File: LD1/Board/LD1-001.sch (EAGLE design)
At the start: 13 parts, among them IC1 TLC5941NT, IC2 TLC5941NT, IC3 TLC5941NT

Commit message: Before the first prototyping.
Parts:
- removed CN2, CN3: (no value), jst-ph:B16B-PH-K-S
- removed SV1: (no value), con-ml:ML10
- added C4: 0.01u, rcl:C-US025-025X050
- added IC4: TLC5941NT, adafruit:TLC5941NT
- added JP1, JP2, JP3, JP4: (no value), pinhead:PINHD-2X16
- added JP5: (no value), pinhead:PINHD-1X2
- added R4: 4.7k, resistor:R-US_0204/5
- CN1: device jst-ph:B16B-PH-K-S -> jst-ph:S8B-PH-K-S
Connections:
- removed net LED2B: CN3.6, IC3.OUT5
- removed net LED2G: CN3.5, IC3.OUT4
- removed net LED3B: CN3.9, IC3.OUT8
- removed net LED3G: CN3.8, IC3.OUT7
- removed net LED3R: CN3.7, IC3.OUT6
- removed net LEDA: CN3.1, IC3.OUT0
- removed net SIN: IC3.SIN, SV1.3
- new net N$37: IC4.IREF, R4.2
- new net N$48: IC3.OUT8, JP3.17
- new net N$49: IC3.OUT9, JP3.19
- new net N$50: IC3.OUT10, JP3.21
- new net N$51: IC3.OUT11, JP3.23
- new net N$52: IC3.OUT12, JP3.25
- new net N$53: IC3.OUT13, JP3.27
- new net N$54: IC3.OUT14, JP3.29
- new net N$55: IC3.OUT15, JP3.31
- new net N$56: IC4.OUT0, JP4.1
- new net N$57: IC4.OUT1, JP4.3
- new net N$58: IC4.OUT2, JP4.5
- new net N$59: IC4.OUT3, JP4.7
- new net N$60: IC4.OUT4, JP4.9
- new net N$61: IC4.OUT5, JP4.11
- new net N$62: IC4.OUT6, JP4.13
- new net N$63: IC4.OUT7, JP4.15
- new net N$64: IC4.OUT8, JP4.17
- new net N$66: IC4.OUT9, JP4.19
- new net N$67: IC4.OUT10, JP4.21
- new net N$68: IC4.OUT11, JP4.23
- new net N$69: IC4.OUT12, JP4.25
- new net N$70: IC4.OUT13, JP4.27
- new net N$71: IC4.OUT14, JP4.29
- new net N$72: IC4.OUT15, JP4.31
- new net N$73: JP1.10, JP1.12, JP1.14, JP1.16, JP1.18, JP1.2, JP1.20, JP1.22, JP1.24, JP1.26, JP1.28, JP1.30, JP1.32, JP1.4, JP1.6, JP1.8, JP2.10, JP2.12, JP2.14, JP2.16, JP2.18, JP2.2, JP2.20, JP2.22, JP2.24, JP2.26, JP2.28, JP2.30, JP2.32, JP2.4, JP2.6, JP2.8, JP3.10, JP3.12, JP3.14, JP3.16, JP3.18, JP3.2, JP3.20, JP3.22, JP3.24, JP3.26, JP3.28, JP3.30, JP3.32, JP3.4, JP3.6, JP3.8, JP4.10, JP4.12, JP4.14, JP4.16, JP4.18, JP4.2, JP4.20, JP4.22, JP4.24, JP4.26, JP4.28, JP4.30, JP4.32, JP4.4, JP4.6, JP4.8, JP5.1
- net BLANK: now also CN1.3, IC4.BLANK; no longer SV1.5
- net GND: now also C4.2, CN1.2, IC4.GND, JP5.2; no longer SV1.10, SV1.2
- net GSCLCK: now also CN1.4, IC4.GSCLK; no longer SV1.7
- net MODE: now also CN1.8, IC4.MODE; no longer SV1.8
- net N$1: now also CN1.6, IC1.SIN; no longer CN2.16, IC2.OUT15
- net N$10: now also IC1.OUT5, JP1.11; no longer IC2.SIN, IC3.SOUT
- net N$11: now also IC1.OUT6, JP1.13; no longer CN2.4, IC2.OUT3
- net N$12: now also IC1.OUT7, JP1.15; no longer CN3.2, IC3.OUT1
- net N$13: now also IC1.OUT8, JP1.17; no longer CN2.5, IC2.OUT4
- net N$14: now also IC1.OUT9, JP1.19; no longer CN3.3, IC3.OUT2
- net N$15: now also IC1.OUT10, JP1.21; no longer CN2.6, IC2.OUT5
- net N$16: now also IC1.OUT11, JP1.23; no longer CN2.7, IC2.OUT6
- net N$17: now also IC1.OUT12, JP1.25; no longer CN2.8, IC2.OUT7
- net N$18: now also IC1.OUT13, JP1.27; no longer CN2.9, IC2.OUT8
- net N$19: now also IC1.OUT14, JP1.29; no longer CN2.10, IC2.OUT9
- net N$2: now also IC1.SOUT, IC2.SIN; no longer CN2.2, IC2.OUT1
- net N$20: now also IC1.OUT15, JP1.31; no longer CN2.11, IC2.OUT10
- net N$21: now also IC2.OUT0, JP2.1; no longer CN2.12, IC2.OUT11
- net N$22: now also IC2.OUT1, JP2.3; no longer CN2.13, IC2.OUT12
- net N$23: now also IC2.OUT2, JP2.5; no longer CN2.14, IC2.OUT13
- net N$24: now also IC2.OUT3, JP2.7; no longer CN3.15, IC3.OUT14
- net N$25: now also IC2.OUT4, JP2.9; no longer CN3.16, IC3.OUT15
- net N$26: now also IC2.OUT5, JP2.11; no longer CN2.15, IC2.OUT14
- net N$27: now also IC2.OUT6, JP2.13; no longer CN2.1, IC2.OUT0
- net N$28: now also IC2.OUT7, JP2.15; no longer CN1.16, IC1.OUT15
- net N$29: now also IC2.OUT8, JP2.17; no longer CN1.15, IC1.OUT14
- net N$3: now also IC2.SOUT, IC3.SIN; no longer CN3.13, IC3.OUT12
- net N$30: now also IC2.OUT9, JP2.19; no longer CN1.14, IC1.OUT13
- net N$31: now also IC2.OUT10, JP2.21; no longer CN1.13, IC1.OUT12
- net N$32: now also IC2.OUT11, JP2.23; no longer CN1.12, IC1.OUT11
- net N$33: now also IC2.OUT12, JP2.25; no longer CN1.11, IC1.OUT10
- net N$34: now also IC2.OUT13, JP2.27; no longer CN1.10, IC1.OUT9
- net N$35: now also IC2.OUT14, JP2.29; no longer CN1.9, IC1.OUT8
- net N$36: now also IC2.OUT15, JP2.31; no longer CN1.8, IC1.OUT7
- net N$38: now also IC3.OUT0, JP3.1; no longer CN1.7, IC1.OUT6
- net N$39: now also IC3.OUT1, JP3.3; no longer CN1.6, IC1.OUT5
- net N$4: now also IC3.SOUT, IC4.SIN; no longer CN2.3, IC2.OUT2
- net N$40: now also IC3.OUT2, JP3.5; no longer CN1.5, IC1.OUT4
- net N$41: now also IC3.OUT3, JP3.7; no longer CN1.4, IC1.OUT3
- net N$42: now also IC3.OUT4, JP3.9; no longer CN1.3, IC1.OUT2
- net N$43: now also IC3.OUT5, JP3.11; no longer CN1.2, IC1.OUT1
- net N$44: now also IC3.OUT6, JP3.13; no longer CN1.1, IC1.OUT0
- net N$45: now also IC3.OUT7, JP3.15; no longer IC1.SIN, IC2.SOUT
- net N$5: now also IC1.OUT0, JP1.1; no longer CN3.14, IC3.OUT13
- net N$6: now also IC1.OUT1, JP1.3; no longer CN3.10, IC3.OUT9
- net N$7: now also IC1.OUT2, JP1.5; no longer CN3.11, IC3.OUT10
- net N$8: now also IC1.OUT3, JP1.7; no longer CN3.12, IC3.OUT11
- net N$9: now also IC1.OUT4, JP1.9; no longer CN3.4, IC3.OUT3
- net SCLCK: now also CN1.7, IC4.SCLK; no longer SV1.4
- net VCC: now also C4.1, CN1.1, IC4.TEST, IC4.VCC, R4.1; no longer SV1.1
- net XLAT: now also CN1.5, IC4.XLAT; no longer SV1.6
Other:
- moved on the sheet: C1, C2, C3, IC1, IC2, IC3, R1, R2, R3

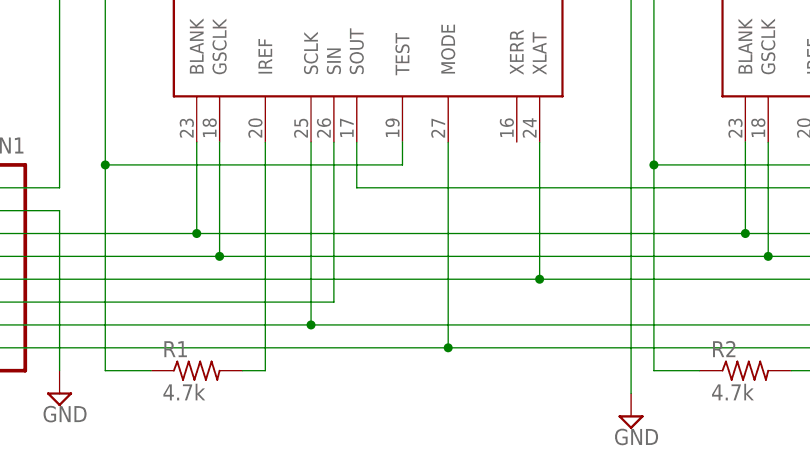
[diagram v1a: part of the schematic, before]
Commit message: Develop for R0.6
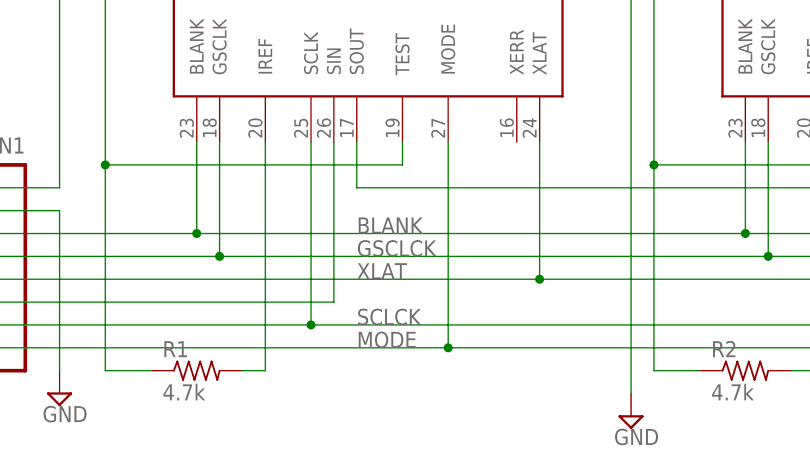
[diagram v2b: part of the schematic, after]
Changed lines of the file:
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@@
 <wire x1="55.88" y1="-68.58" x2="-5.08" y2="-68.58" width="0.1524" layer="91"/>
 <junction x="55.88" y="-68.58"/>
+<label x="35.56" y="-68.58" size="1.778" layer="95"/>
 </segment>
 </net>
@@
 <wire x1="45.72" y1="-76.2" x2="-5.08" y2="-76.2" width="0.1524" layer="91"/>
 <junction x="45.72" y="-76.2"/>
+<label x="35.56" y="-76.2" size="1.778" layer="95"/>
 </segment>
 </net>
@@
 <wire x1="17.78" y1="-63.5" x2="-5.08" y2="-63.5" width="0.1524" layer="91"/>
 <junction x="17.78" y="-63.5"/>
+<label x="35.56" y="-63.5" size="1.778" layer="95"/>
 </segment>
 </net>
@@
 <wire x1="30.48" y1="-73.66" x2="-5.08" y2="-73.66" width="0.1524" layer="91"/>
 <junction x="30.48" y="-73.66"/>
+<label x="35.56" y="-73.66" size="1.778" layer="95"/>
 </segment>
 </net>
@@
 <wire x1="20.32" y1="-66.04" x2="-5.08" y2="-66.04" width="0.1524" layer="91"/>
 <junction x="20.32" y="-66.04"/>
+<label x="35.56" y="-66.04" size="1.778" layer="95"/>
 </segment>
 </net>

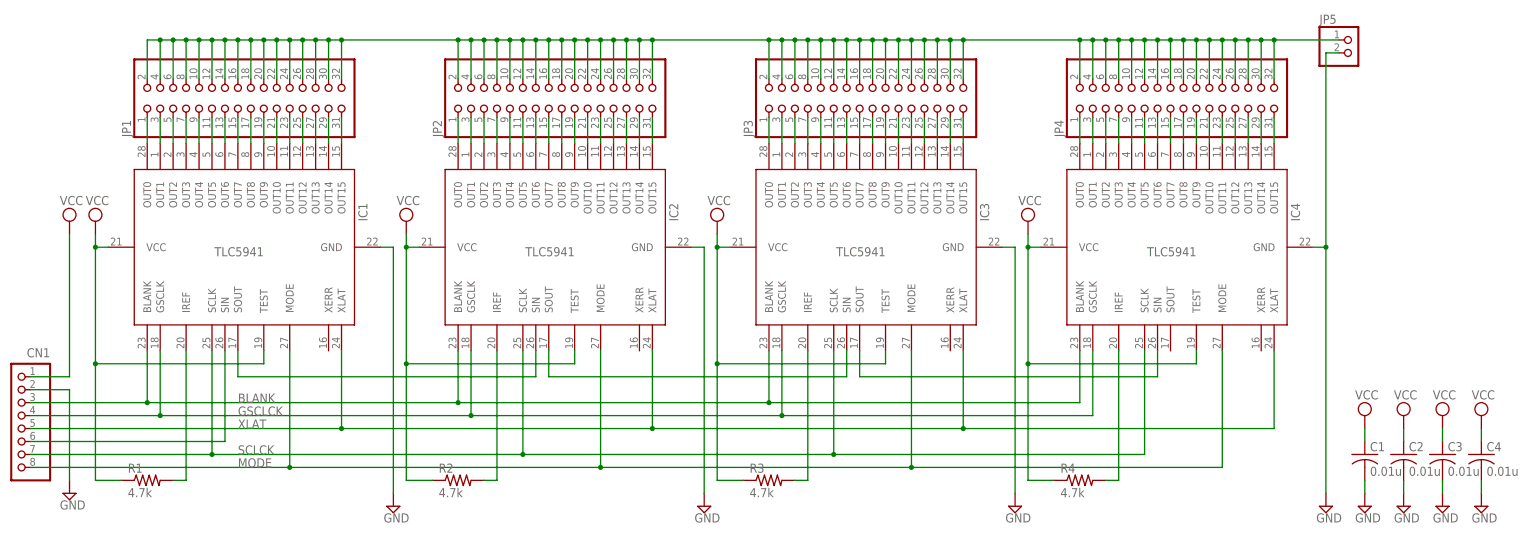
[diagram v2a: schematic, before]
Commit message: Removed D2 and D7.
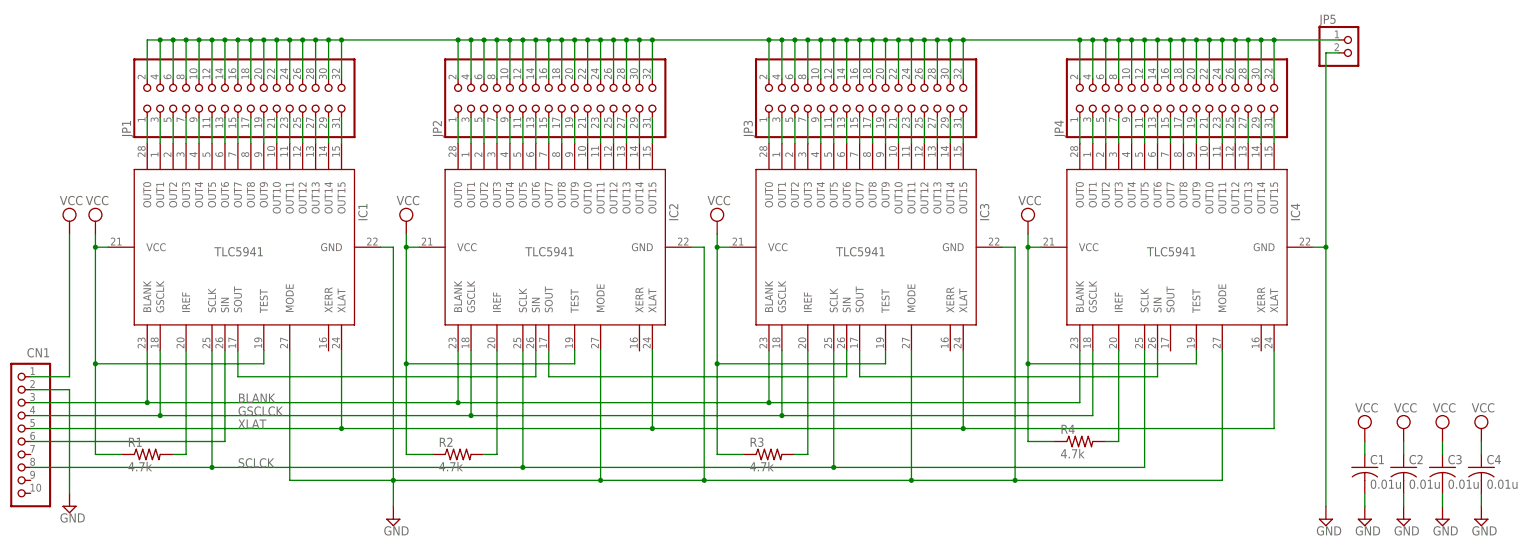
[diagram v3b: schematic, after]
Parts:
- CN1: device jst-ph:S8B-PH-K-S -> jst-ph:S10B-PH-K-S
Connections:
- removed net MODE: CN1.8, IC1.MODE, IC2.MODE, IC3.MODE, IC4.MODE
- net GND: now also IC1.MODE, IC2.MODE, IC3.MODE, IC4.MODE
- net SCLCK: now also CN1.8; no longer CN1.7
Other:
- moved on the sheet: C1, C2, C3, C4, R1, R2, R3, R4

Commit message: Updated LD1.
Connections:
- new net N$75: CN1.9, IC1.MODE, IC2.MODE, IC3.MODE, IC4.MODE
- net GND: no longer IC1.MODE, IC2.MODE, IC3.MODE, IC4.MODE
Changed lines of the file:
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@@
 <part name="JP4" library="pinhead" deviceset="PINHD-2X16" device=""/>
 <part name="JP5" library="pinhead" deviceset="PINHD-1X2" device=""/>
+<part name="SUPPLY6" library="supply2" deviceset="GND" device=""/>
+<part name="SUPPLY8" library="supply2" deviceset="GND" device=""/>
 </parts>
 <sheets>
@@
 <instance part="JP4" gate="A" x="218.44" y="-5.08" rot="R90"/>
 <instance part="JP5" gate="G$1" x="254" y="5.08"/>
+<instance part="SUPPLY6" gate="GND" x="127" y="-86.36"/>
+<instance part="SUPPLY8" gate="GND" x="187.96" y="-86.36"/>
 </instances>
 <busses>
@@
 </segment>
 <segment>
-<pinref part="IC2" gate="G$1" pin="GND"/>
-<wire x1="124.46" y1="-33.02" x2="127" y2="-33.02" width="0.1524" layer="91"/>
-<wire x1="127" y1="-33.02" x2="127" y2="-78.74" width="0.1524" layer="91"/>
-<pinref part="IC1" gate="G$1" pin="GND"/>
-<wire x1="63.5" y1="-33.02" x2="66.04" y2="-33.02" width="0.1524" layer="91"/>
-<wire x1="66.04" y1="-33.02" x2="66.04" y2="-78.74" width="0.1524" layer="91"/>
-<pinref part="SUPPLY4" gate="GND" pin="GND"/>
-<pinref part="IC4" gate="G$1" pin="MODE"/>
-<wire x1="66.04" y1="-78.74" x2="66.04" y2="-83.82" width="0.1524" layer="91"/>
-<wire x1="228.6" y1="-78.74" x2="228.6" y2="-53.34" width="0.1524" layer="91"/>
-<wire x1="106.68" y1="-78.74" x2="127" y2="-78.74" width="0.1524" layer="91"/>
-<wire x1="127" y1="-78.74" x2="167.64" y2="-78.74" width="0.1524" layer="91"/>
-<wire x1="167.64" y1="-78.74" x2="187.96" y2="-78.74" width="0.1524" layer="91"/>
-<pinref part="IC3" gate="G$1" pin="MODE"/>
-<wire x1="187.96" y1="-78.74" x2="228.6" y2="-78.74" width="0.1524" layer="91"/>
-<wire x1="167.64" y1="-53.34" x2="167.64" y2="-78.74" width="0.1524" layer="91"/>
-<pinref part="IC2" gate="G$1" pin="MODE"/>
-<wire x1="106.68" y1="-53.34" x2="106.68" y2="-78.74" width="0.1524" layer="91"/>
-<junction x="167.64" y="-78.74"/>
-<pinref part="IC1" gate="G$1" pin="MODE"/>
-<wire x1="45.72" y1="-53.34" x2="45.72" y2="-78.74" width="0.1524" layer="91"/>
-<wire x1="106.68" y1="-78.74" x2="66.04" y2="-78.74" width="0.1524" layer="91"/>
-<junction x="106.68" y="-78.74"/>
-<junction x="66.04" y="-78.74"/>
-<wire x1="66.04" y1="-78.74" x2="45.72" y2="-78.74" width="0.1524" layer="91"/>
-<junction x="127" y="-78.74"/>
-<pinref part="IC3" gate="G$1" pin="GND"/>
-<wire x1="185.42" y1="-33.02" x2="187.96" y2="-33.02" width="0.1524" layer="91"/>
-<wire x1="187.96" y1="-33.02" x2="187.96" y2="-78.74" width="0.1524" layer="91"/>
-<junction x="187.96" y="-78.74"/>
-</segment>
-<segment>
 <pinref part="CN1" gate="G$1" pin="2"/>
 <wire x1="-5.08" y1="-60.96" x2="2.54" y2="-60.96" width="0.1524" layer="91"/>
@@
 <pinref part="SUPPLY18" gate="GND" pin="GND"/>
 <wire x1="279.4" y1="-81.28" x2="279.4" y2="-83.82" width="0.1524" layer="91"/>
+</segment>
+<segment>
+<pinref part="IC1" gate="G$1" pin="GND"/>
+<wire x1="63.5" y1="-33.02" x2="66.04" y2="-33.02" width="0.1524" layer="91"/>
+<pinref part="SUPPLY4" gate="GND" pin="GND"/>
+<wire x1="66.04" y1="-33.02" x2="66.04" y2="-83.82" width="0.1524" layer="91"/>
+</segment>
+<segment>
+<pinref part="IC2" gate="G$1" pin="GND"/>
+<wire x1="124.46" y1="-33.02" x2="127" y2="-33.02" width="0.1524" layer="91"/>
+<wire x1="127" y1="-33.02" x2="127" y2="-83.82" width="0.1524" layer="91"/>
+<pinref part="SUPPLY6" gate="GND" pin="GND"/>
+</segment>
+<segment>
+<pinref part="IC3" gate="G$1" pin="GND"/>
+<wire x1="185.42" y1="-33.02" x2="187.96" y2="-33.02" width="0.1524" layer="91"/>
+<wire x1="187.96" y1="-33.02" x2="187.96" y2="-83.82" width="0.1524" layer="91"/>
+<pinref part="SUPPLY8" gate="GND" pin="GND"/>
 </segment>
 </net>
@@
 </segment>
 </net>
+<net name="N$75" class="0">
+<segment>
+<pinref part="IC4" gate="G$1" pin="MODE"/>
+<wire x1="228.6" y1="-78.74" x2="228.6" y2="-53.34" width="0.1524" layer="91"/>
+<wire x1="106.68" y1="-78.74" x2="167.64" y2="-78.74" width="0.1524" layer="91"/>
+<pinref part="IC3" gate="G$1" pin="MODE"/>
+<wire x1="167.64" y1="-78.74" x2="228.6" y2="-78.74" width="0.1524" layer="91"/>
+<wire x1="167.64" y1="-53.34" x2="167.64" y2="-78.74" width="0.1524" layer="91"/>
+<pinref part="IC2" gate="G$1" pin="MODE"/>
+<wire x1="106.68" y1="-53.34" x2="106.68" y2="-78.74" width="0.1524" layer="91"/>
+<junction x="167.64" y="-78.74"/>
+<pinref part="IC1" gate="G$1" pin="MODE"/>
+<wire x1="45.72" y1="-53.34" x2="45.72" y2="-78.74" width="0.1524" layer="91"/>
+<wire x1="106.68" y1="-78.74" x2="45.72" y2="-78.74" width="0.1524" layer="91"/>
+<junction x="106.68" y="-78.74"/>
+<pinref part="CN1" gate="G$1" pin="9"/>
+<wire x1="45.72" y1="-78.74" x2="-5.08" y2="-78.74" width="0.1524" layer="91"/>
+<junction x="45.72" y="-78.74"/>
+</segment>
+</net>
